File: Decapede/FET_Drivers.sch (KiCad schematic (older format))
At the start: 40 parts, among them J10 FET3, J11 FET4, J8 FET1, J9 FET2, Q10 BC807,215, Q11 BC817-25,215, Q12 BC817-25,215, Q13 PSMN023-40YLCX, Q14 PSMN023-40YLCX, Q15 BC807,215, Q16 BC807,215, Q5 BC817-25,215, Q6 BC817-25,215, Q7 PSMN023-40YLCX, Q8 PSMN023-40YLCX, Q9 BC807,215

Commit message: Updates for Decapede project.
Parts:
- removed D5, D6, D8: Diode 10TQ035, ~, symbol DIODESCH
- added D16, D17, D19: ES1D, ~, symbol DIODESCH
- added D18, D5, D6, D8: LED, ~, symbol LED
- D7: value Diode 10TQ035 -> ES1D
- Q13, Q14, Q7, Q8: symbol BUK7226-75A -> PSMN023-40YLCX
- R56, R58, R65, R68: value 30 Ohm -> 1k8
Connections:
- net +12V: now also R56.1, R58.1, R65.1, R68.1
- net +24V: now also D7.2 (K), D16.2 (K), D17.2 (K), D19.2 (K)
- net FET1: now also R57.1
- net FET2: now also R60.1
- net FET3: now also R67.1
- net FET4: now also R70.1
- net GND: now also Q13.1 (S), Q14.1 (S), Q7.1 (S), Q8.1 (S); no longer D7.1 (A), Q13.3 (S), Q14.3 (S), Q7.3 (S), Q8.3 (S)
- net at Q15.2 (E), R66.2: no longer R65.2
- net FET3_OUT: now reaches J10.2 (PM)
- net FET3_OUT: now also Q13.5 (D), D18.2 (K), D19.1 (A); no longer Q13.2 (D)
- net at Q16.2 (E), R69.2: no longer R68.2
- net FET_OUT4: now reaches J11.2 (PM)
- net FET_OUT4: now also Q14.5 (D), D17.1 (A), D8.2 (K); no longer Q14.2 (D)
- net at R51.1: now also Q7.4 (G), R55.2; no longer Q5.2 (E)
- net FET1_OUT: now reaches J8.2 (PM)
- net FET1_OUT: now also Q7.5 (D), D16.1 (A), D5.2 (K); no longer Q7.2 (D)
- net at Q10.2 (E), R59.2: no longer R58.2
- net FET2_OUT: now reaches J9.2 (PM)
- net FET2_OUT: now also D7.1 (A), Q8.5 (D), D6.2 (K); no longer Q8.2 (D)
- new net: Q13.4 (G), R61.2, R66.1
- new net: Q14.4 (G), R62.2, R69.1
- new net: Q5.2 (E), R51.2
- new net: D5.1 (A), R56.2
- new net: Q9.2 (E), R55.1
- new net: Q8.4 (G), R52.2, R59.1
- new net: D8.1 (A), R65.2
- new net: D18.1 (A), R68.2
- new net: D6.1 (A), R58.2
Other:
- moved on the sheet: J10, J11, Q11, Q12, Q13, Q14, Q15, Q16, Q7, Q9, R51, R55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

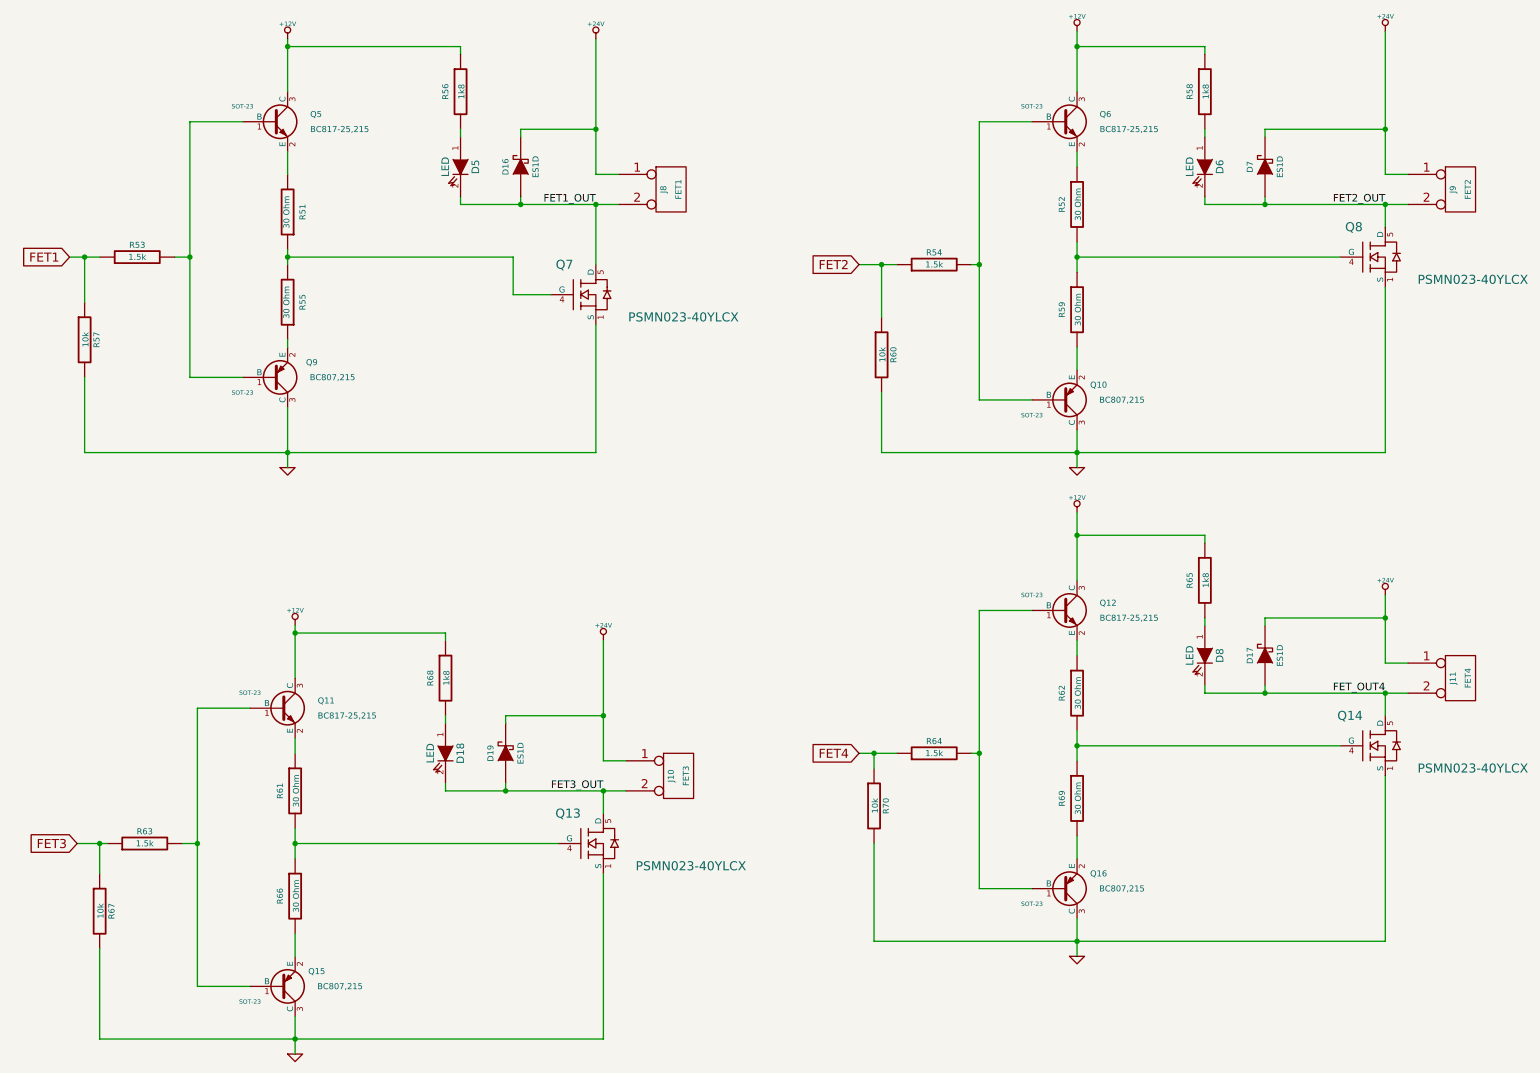
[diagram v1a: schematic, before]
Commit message: Decapede update: add fuses for each main section; change endstops to use 0V instead of 5V; more space for stepper drivers to allow latching connectors
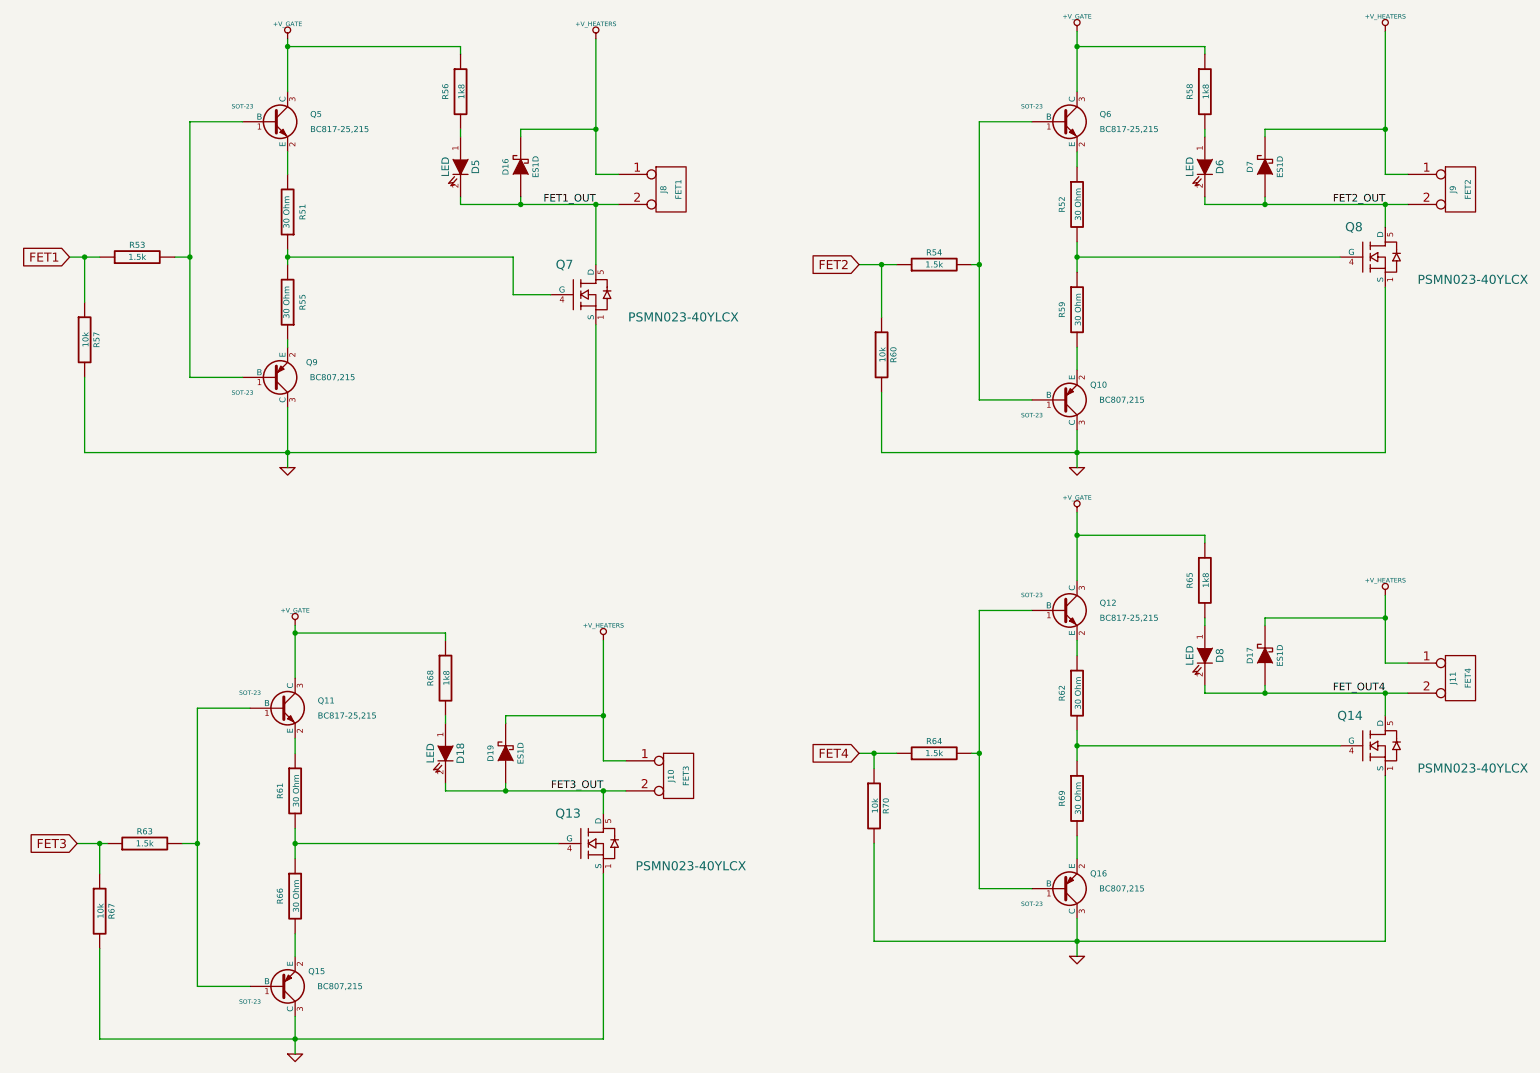
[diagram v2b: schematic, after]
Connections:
- net +12V renamed +V_GATE
- net +24V renamed +V_HEATERS
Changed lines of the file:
@@
 Sheet 6 10
 Title "FET Driver Stage"
-Date "26 jan 2014"
+Date "30 jan 2014"
 Rev ""
 Comp ""
@@
 $EndComp
 $Comp
-L +12V #PWR0131
-U 1 1 52DC411A
-P 2300 750
-F 0 "#PWR0131" H 2300 700 20  0001 C CNN
-F 1 "+12V" H 2300 850 30  0000 C CNN
-F 2 "" H 2300 750 60  0000 C CNN
-F 3 "" H 2300 750 60  0000 C CNN
-	1    2300 750
-	1    0    0    -1
-$EndComp
-$Comp
-L GND #PWR0132
+L GND #PWR0135
 U 1 1 52DC4120
 P 2300 3600
-F 0 "#PWR0132" H 2300 3600 30  0001 C CNN
+F 0 "#PWR0135" H 2300 3600 30  0001 C CNN
 F 1 "GND" H 2300 3530 30  0001 C CNN
 F 2 "" H 2300 3600 60  0000 C CNN
@@
 F 3 "" H 4850 1750 60  0000 C CNN
 	1    4850 1750
-	1    0    0    -1
-$EndComp
-$Comp
-L +24V #PWR0133
-U 1 1 52DC4171
-P 4350 750
-F 0 "#PWR0133" H 4350 700 20  0001 C CNN
-F 1 "+24V" H 4350 850 30  0000 C CNN
-F 2 "" H 4350 750 60  0000 C CNN
-F 3 "" H 4350 750 60  0000 C CNN
-	1    4350 750
 	1    0    0    -1
 $EndComp
@@
 $EndComp
 $Comp
-L +12V #PWR0134
-U 1 1 52DC440F
-P 7550 700
-F 0 "#PWR0134" H 7550 650 20  0001 C CNN
-F 1 "+12V" H 7550 800 30  0000 C CNN
-F 2 "" H 7550 700 60  0000 C CNN
-F 3 "" H 7550 700 60  0000 C CNN
-	1    7550 700
-	1    0    0    -1
-$EndComp
-$Comp
-L GND #PWR0135
+L GND #PWR0136
 U 1 1 52DC4415
 P 7550 3600
-F 0 "#PWR0135" H 7550 3600 30  0001 C CNN
+F 0 "#PWR0136" H 7550 3600 30  0001 C CNN
 F 1 "GND" H 7550 3530 30  0001 C CNN
 F 2 "" H 7550 3600 60  0000 C CNN
@@
 F 3 "" H 10100 1750 60  0000 C CNN
 	1    10100 1750
-	1    0    0    -1
-$EndComp
-$Comp
-L +24V #PWR0136
-U 1 1 52DC4449
-P 9600 700
-F 0 "#PWR0136" H 9600 650 20  0001 C CNN
-F 1 "+24V" H 9600 800 30  0000 C CNN
-F 2 "" H 9600 700 60  0000 C CNN
-F 3 "" H 9600 700 60  0000 C CNN
-	1    9600 700
 	1    0    0    -1
 $EndComp
@@
 $EndComp
 $Comp
-L +12V #PWR0137
-U 1 1 52DC2427
-P 2350 4650
-F 0 "#PWR0137" H 2350 4600 20  0001 C CNN
-F 1 "+12V" H 2350 4750 30  0000 C CNN
-F 2 "" H 2350 4650 60  0000 C CNN
-F 3 "" H 2350 4650 60  0000 C CNN
-	1    2350 4650
-	1    0    0    -1
-$EndComp
-$Comp
-L GND #PWR0138
+L GND #PWR0137
 U 1 1 52DC242D
 P 2350 7500
-F 0 "#PWR0138" H 2350 7500 30  0001 C CNN
+F 0 "#PWR0137" H 2350 7500 30  0001 C CNN
 F 1 "GND" H 2350 7430 30  0001 C CNN
 F 2 "" H 2350 7500 60  0000 C CNN
@@
 F 3 "" H 4900 5650 60  0000 C CNN
 	1    4900 5650
-	1    0    0    -1
-$EndComp
-$Comp
-L +24V #PWR0139
-U 1 1 52DC2461
-P 4400 4750
-F 0 "#PWR0139" H 4400 4700 20  0001 C CNN
-F 1 "+24V" H 4400 4850 30  0000 C CNN
-F 2 "" H 4400 4750 60  0000 C CNN
-F 3 "" H 4400 4750 60  0000 C CNN
-	1    4400 4750
 	1    0    0    -1
 $EndComp
@@
 $EndComp
 $Comp
-L +12V #PWR0140
-U 1 1 52DC249F
-P 7550 3900
-F 0 "#PWR0140" H 7550 3850 20  0001 C CNN
-F 1 "+12V" H 7550 4000 30  0000 C CNN
-F 2 "" H 7550 3900 60  0000 C CNN
-F 3 "" H 7550 3900 60  0000 C CNN
-	1    7550 3900
-	1    0    0    -1
-$EndComp
-$Comp
-L GND #PWR0141
+L GND #PWR0138
 U 1 1 52DC24A5
 P 7550 6850
-F 0 "#PWR0141" H 7550 6850 30  0001 C CNN
+F 0 "#PWR0138" H 7550 6850 30  0001 C CNN
 F 1 "GND" H 7550 6780 30  0001 C CNN
 F 2 "" H 7550 6850 60  0000 C CNN
@@
 F 3 "" H 10100 5000 60  0000 C CNN
 	1    10100 5000
-	1    0    0    -1
-$EndComp
-$Comp
-L +24V #PWR0142
-U 1 1 52DC24DA
-P 9600 4450
-F 0 "#PWR0142" H 9600 4400 20  0001 C CNN
-F 1 "+24V" H 9600 4550 30  0000 C CNN
-F 2 "" H 9600 4450 60  0000 C CNN
-F 3 "" H 9600 4450 60  0000 C CNN
-	1    9600 4450
 	1    0    0    -1
 $EndComp
@@
 	3800 2450 4050 2450
 Connection ~ 2300 2200
+$Comp
+L +V_GATE #PWR0139
+U 1 1 52E8361C
+P 2300 750
+F 0 "#PWR0139" H 2300 720 30  0001 C CNN
+F 1 "+V_GATE" H 2300 850 30  0000 C CNN
+F 2 "~" H 2300 750 60  0000 C CNN
+F 3 "~" H 2300 750 60  0000 C CNN
+	1    2300 750
+	1    0    0    -1
+$EndComp
+$Comp
+L +V_GATE #PWR0140
+U 1 1 52E83629
+P 7550 700
+F 0 "#PWR0140" H 7550 670 30  0001 C CNN
+F 1 "+V_GATE" H 7550 800 30  0000 C CNN
+F 2 "~" H 7550 700 60  0000 C CNN
+F 3 "~" H 7550 700 60  0000 C CNN
+	1    7550 700
+	1    0    0    -1
+$EndComp
+$Comp
+L +V_GATE #PWR0141
+U 1 1 52E8362F
+P 7550 3900
+F 0 "#PWR0141" H 7550 3870 30  0001 C CNN
+F 1 "+V_GATE" H 7550 4000 30  0000 C CNN
+F 2 "~" H 7550 3900 60  0000 C CNN
+F 3 "~" H 7550 3900 60  0000 C CNN
+	1    7550 3900
+	1    0    0    -1
+$EndComp
+$Comp
+L +V_GATE #PWR0142
+U 1 1 52E83635
+P 2350 4650
+F 0 "#PWR0142" H 2350 4620 30  0001 C CNN
+F 1 "+V_GATE" H 2350 4750 30  0000 C CNN
+F 2 "~" H 2350 4650 60  0000 C CNN
+F 3 "~" H 2350 4650 60  0000 C CNN
+	1    2350 4650
+	1    0    0    -1
+$EndComp
+$Comp
+L +V_HEATERS #PWR0143
+U 1 1 52E8363D
+P 4350 750
+F 0 "#PWR0143" H 4350 720 30  0001 C CNN
+F 1 "+V_HEATERS" H 4350 850 30  0000 C CNN
+F 2 "~" H 4350 750 60  0000 C CNN
+F 3 "~" H 4350 750 60  0000 C CNN
+	1    4350 750
+	1    0    0    -1
+$EndComp
+$Comp
+L +V_HEATERS #PWR0144
+U 1 1 52E8364C
+P 9600 700
+F 0 "#PWR0144" H 9600 670 30  0001 C CNN
+F 1 "+V_HEATERS" H 9600 800 30  0000 C CNN
+F 2 "~" H 9600 700 60  0000 C CNN
+F 3 "~" H 9600 700 60  0000 C CNN
+	1    9600 700
+	1    0    0    -1
+$EndComp
+$Comp
+L +V_HEATERS #PWR0145
+U 1 1 52E8365B
+P 4400 4750
+F 0 "#PWR0145" H 4400 4720 30  0001 C CNN
+F 1 "+V_HEATERS" H 4400 4850 30  0000 C CNN
+F 2 "~" H 4400 4750 60  0000 C CNN
+F 3 "~" H 4400 4750 60  0000 C CNN
+	1    4400 4750
+	1    0    0    -1
+$EndComp
+$Comp
+L +V_HEATERS #PWR0146
+U 1 1 52E8366A
+P 9600 4450
+F 0 "#PWR0146" H 9600 4420 30  0001 C CNN
+F 1 "+V_HEATERS" H 9600 4550 30  0000 C CNN
+F 2 "~" H 9600 4450 60  0000 C CNN
+F 3 "~" H 9600 4450 60  0000 C CNN
+	1    9600 4450
+	1    0    0    -1
+$EndComp
 $EndSCHEMATC
